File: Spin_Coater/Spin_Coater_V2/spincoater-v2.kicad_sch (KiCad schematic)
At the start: 36 parts, among them J1 KEYPAD, J2 POT_PIN28, J3 SDCARD, J4 POT_PIN27, J5 MOTOR, J6 LED1, J7 LED2, J8 12V_DC, J9 LCD, Q1 IRF9540N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

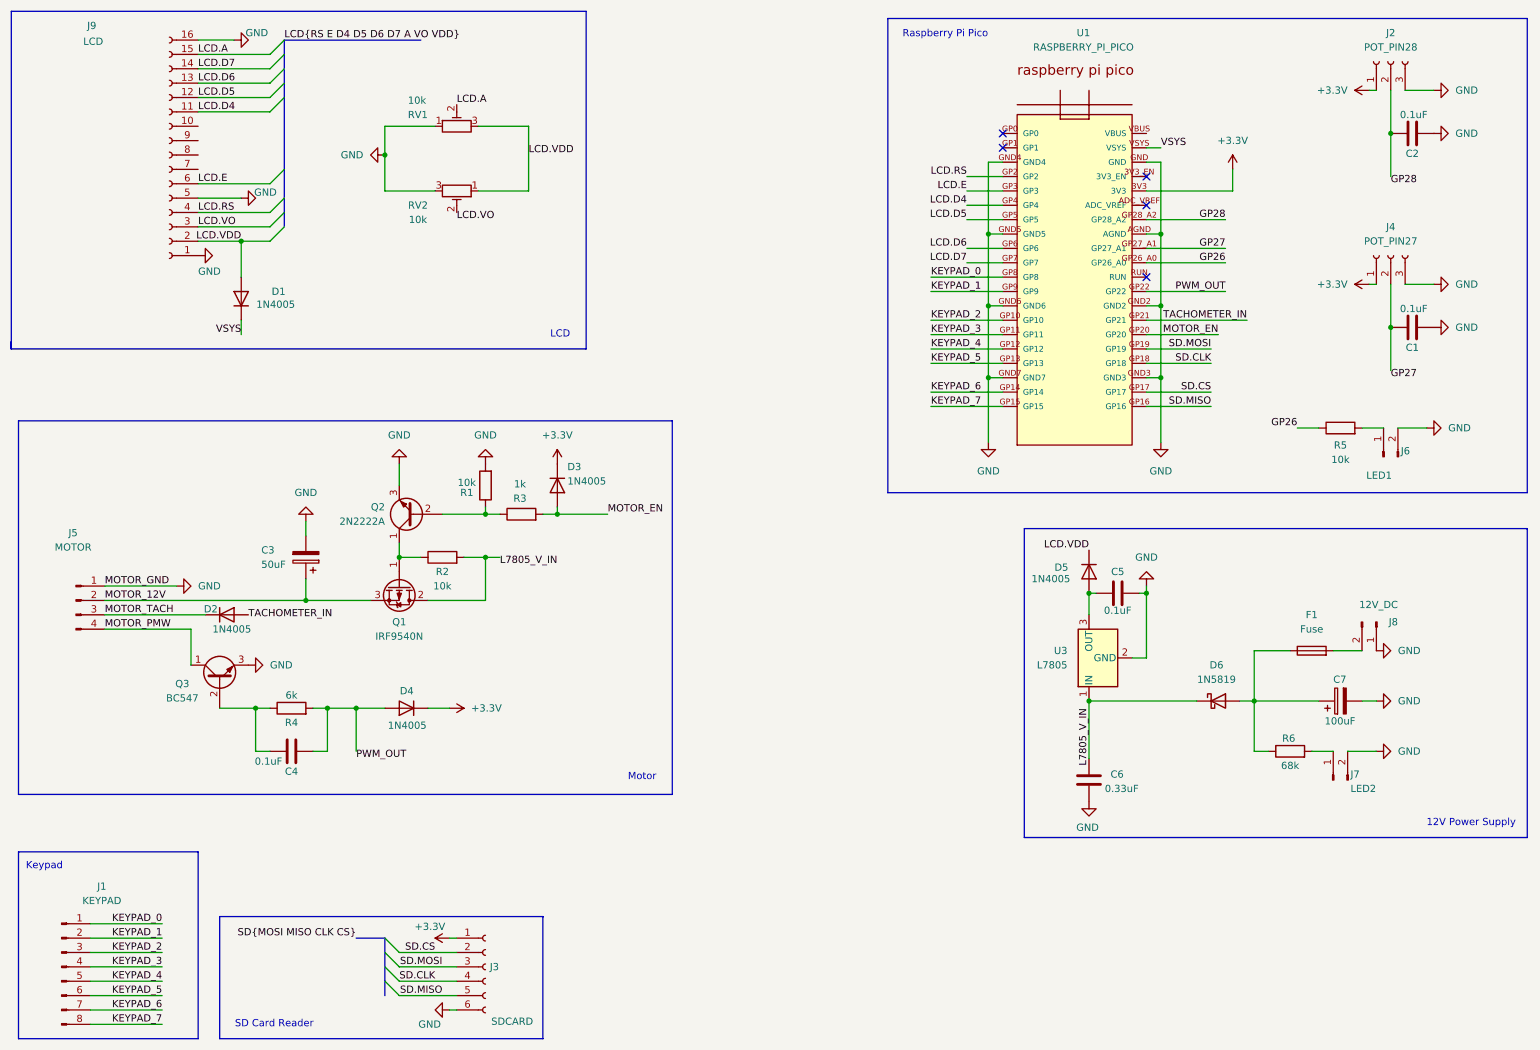
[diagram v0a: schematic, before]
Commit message: Added interferometer project, recorded some simulation stats in README file
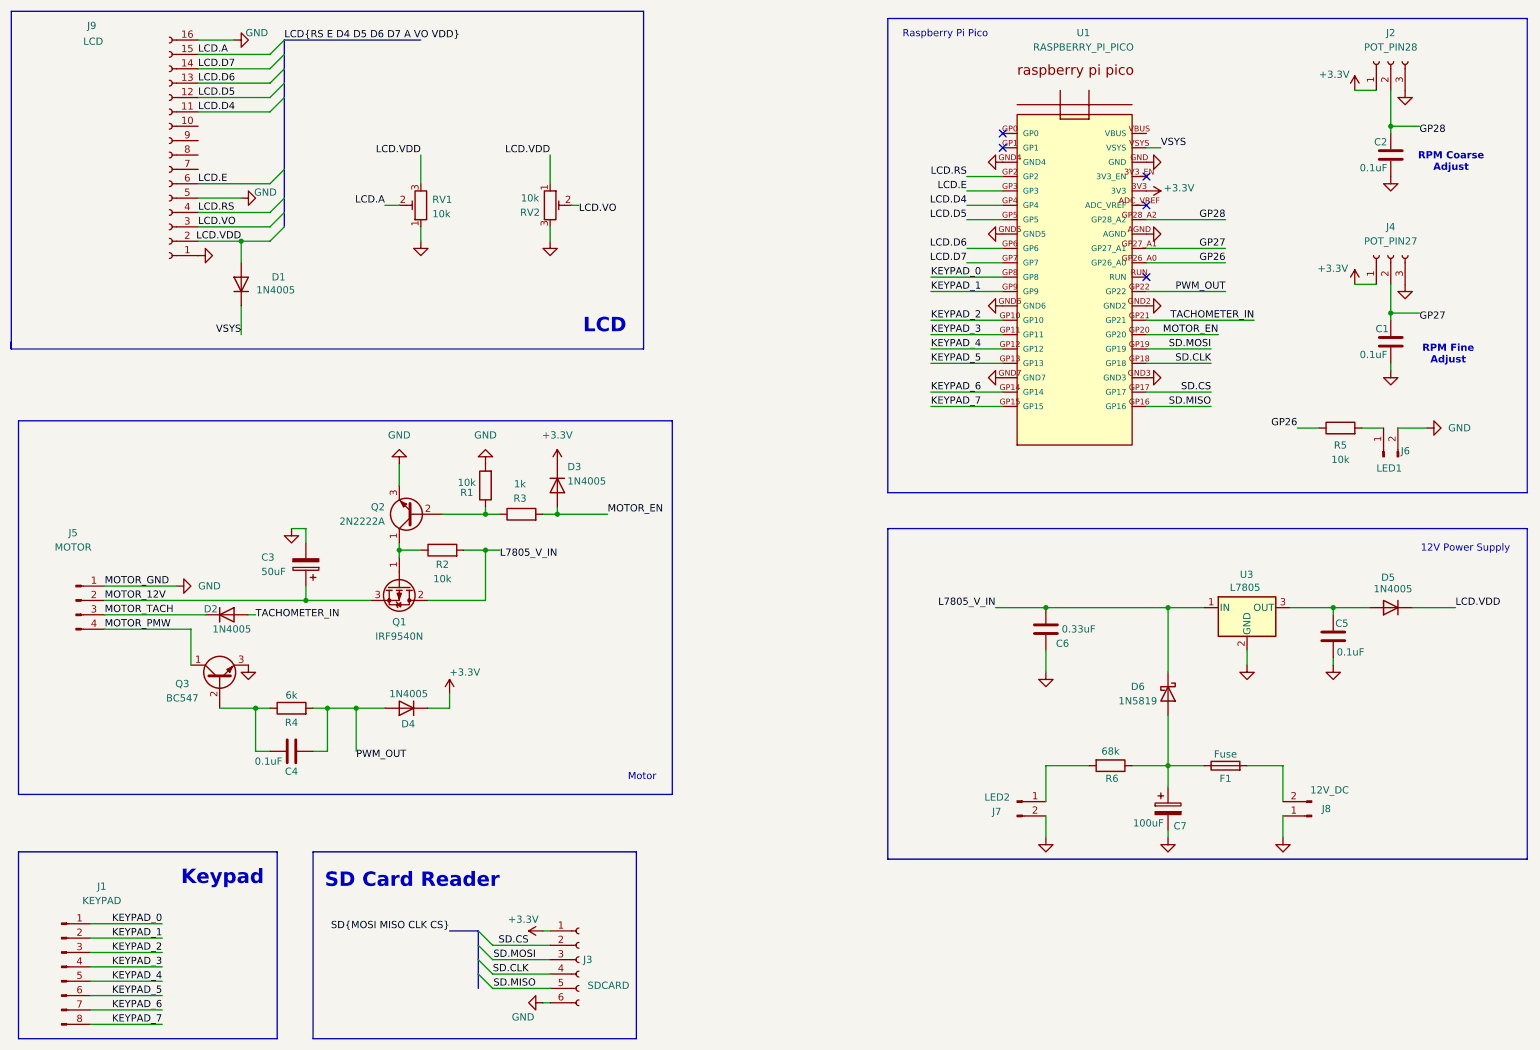
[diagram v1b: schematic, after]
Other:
- note added: "RPM Coarse Adjust"
- note added: "RPM Fine Adjust"
- moved on the sheet: C1, C2, C3, C5, C6, C7, D1, D5, D6, F1, J3, J7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
